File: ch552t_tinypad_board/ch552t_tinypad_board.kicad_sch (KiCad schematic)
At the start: 19 parts, among them J1 Conn_02x10_Odd_Even, J2 Conn_01x02_Pin, J3 USB_C_Receptacle_USB2.0, SW1 SW_Push, SW2 SW_Push, SW3 SW_Push, SW4 SW_Push, SW5 SW_Push, SW6 SW_Push, U1 CH552T

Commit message: feat: auto wiring and board outline
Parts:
- removed J2: Conn_01x02_Pin, Connector_PinHeader_2.54mm:PinHeader_1x02_P2.54mm_Vertical, symbol Connector:Conn_01x02_Pin
- added SW7: SW_Push, Library:SW_SPST_TVAF06_A020B_R, symbol Switch:SW_Push
- C1, C2: footprint Capacitor_SMD:C_0603_1608Metric_Pad1.08x0.95mm_HandSolder -> Library:C_SMD_0603_1608_Disc_DualUse
- D1: footprint LED_SMD:LED_0603_1608Metric_Pad1.05x0.95mm_HandSolder -> LED_THT:LED_D3.0mm
- R1, R2: footprint Resistor_SMD:R_0603_1608Metric_Pad0.98x0.95mm_HandSolder -> Library:R_SMD_0603_1608_THT_DIN0207_DualUse
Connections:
- net P1.4: no longer SW4.1
- net P3.0: now also SW4.1
- net at R2.2: now also SW7.2
- net P3.6 renamed D+
- net D+: now also SW7.1
- net P3.7 renamed D-

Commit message: feat: connect keys to MCU
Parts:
- removed H1, H2, H3, H4: MountingHole, MountingHole:MountingHole_3.2mm_M3, symbol Mechanical:MountingHole
- added H1, H2, H3, H4: MountingHole_Pad, MountingHole:MountingHole_3.2mm_M3_Pad_Via, symbol Mechanical:MountingHole_Pad
- renumbered J3 to J2
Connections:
- net GND: now also H1.1, H2.1, H3.1, H4.1
- net P1.0: no longer SW2.1
- net P1.1: now also SW6.1; no longer SW1.1
- net P1.5: no longer SW5.1
- net P1.6: no longer SW6.1
- net P1.7: no longer SW3.1
- net P3.1: now also SW5.1
- net P3.2: no longer D1.2 (A)
- net P3.3: now also SW1.1
- net P3.4: now also SW2.1
- net P3.5: now also SW3.1
- no-connect marks 4 -> 6

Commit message: fix: pulldown CC pins on USB-C
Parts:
- added R3, R4: R, Library:R_SMD_0603_1608_THT_DIN0207_DualUse, symbol Device:R
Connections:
- net GND: now also R3.2, R4.2
- net at J2.A5 (CC1): now also R4.1
- net at J2.B5 (CC2): now also R3.1
- no-connect marks 6 -> 4
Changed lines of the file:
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@@
   (junction (at 66.04 50.8) (diameter 0) (color 0 0 0 0)
   )
-  (no_connect (at 199.39 26.67))
   (no_connect (at 170.18 100.33))
   (no_connect (at 199.39 49.53))
-  (no_connect (at 199.39 29.21))
   (no_connect (at 199.39 52.07))
   (no_connect (at 176.53 90.17))
+  (wire (pts (xy 234.95 29.21) (xy 234.95 26.67))
+    (stroke (width 0) (type default))
+  )
   (wire (pts (xy 184.15 90.17) (xy 194.31 90.17))
     (stroke (width 0) (type default))
@@
     (stroke (width 0) (type default))
   )
+  (wire (pts (xy 226.06 36.83) (xy 226.06 39.37))
+    (stroke (width 0) (type default))
+  )
   (wire (pts (xy 210.82 82.55) (xy 144.78 82.55))
     (stroke (width 0) (type default))
@@
     (stroke (width 0) (type default))
   )
+  (wire (pts (xy 234.95 36.83) (xy 234.95 39.37))
+    (stroke (width 0) (type default))
+  )
+  (wire (pts (xy 234.95 26.67) (xy 199.39 26.67))
+    (stroke (width 0) (type default))
+  )
   (wire (pts (xy 184.15 59.69) (xy 184.15 62.23))
     (stroke (width 0) (type default))
@@
   )
   (wire (pts (xy 144.78 69.85) (xy 173.99 69.85))
+    (stroke (width 0) (type default))
+  )
+  (wire (pts (xy 199.39 29.21) (xy 226.06 29.21))
     (stroke (width 0) (type default))
   )
@@
     )
   )
+  (symbol (lib_id "power:GND") (at 226.06 39.37 0) (unit 1)
+    (in_bom yes) (on_board yes) (dnp no) (fields_autoplaced)
+    (property "Reference" "#PWR016" (at 226.06 45.72 0)
+      (effects (font (size 1.27 1.27)) hide)
+    )
+    (property "Value" "GND" (at 226.06 44.45 0)
+      (effects (font (size 1.27 1.27)))
+    )
+    (property "Footprint" "" (at 226.06 39.37 0)
+      (effects (font (size 1.27 1.27)) hide)
+    )
+    (property "Datasheet" "" (at 226.06 39.37 0)
+      (effects (font (size 1.27 1.27)) hide)
+    )
+    (pin "1")
+    (instances
+      (project "ch552t_tinypad_board"
+        (path "/12a9bd1e-67e4-4b41-b498-ff4d6b2646d2"
+          (reference "#PWR016") (unit 1)
+        )
+      )
+    )
+  )
   (symbol (lib_id "power:VCC") (at 173.99 69.85 0) (unit 1)
     (in_bom yes) (on_board yes) (dnp no) (fields_autoplaced)
@@
         (path "/56328475-aff9-4d2d-8d78-1ad1f91ab129"
           (reference "#PWR05") (unit 1)
+        )
+      )
+    )
+  )
+  (symbol (lib_id "Device:R") (at 234.95 33.02 0) (unit 1)
+    (in_bom yes) (on_board yes) (dnp no) (fields_autoplaced)
+    (property "Reference" "R4" (at 237.49 31.75 0)
+      (effects (font (size 1.27 1.27)) (justify left))
+    )
+    (property "Value" "R" (at 237.49 34.29 0)
+      (effects (font (size 1.27 1.27)) (justify left))
+    )
+    (property "Footprint" "Library:R_SMD_0603_1608_THT_DIN0207_DualUse" (at 233.172 33.02 90)
+      (effects (font (size 1.27 1.27)) hide)
+    )
+    (property "Datasheet" "~" (at 234.95 33.02 0)
+      (effects (font (size 1.27 1.27)) hide)
+    )
+    (pin "1")
+    (pin "2")
+    (instances
+      (project "ch552t_tinypad_board"
+        (path "/12a9bd1e-67e4-4b41-b498-ff4d6b2646d2"
+          (reference "R4") (unit 1)
         )
       )
@@
     )
   )
+  (symbol (lib_id "Device:R") (at 226.06 33.02 0) (unit 1)
+    (in_bom yes) (on_board yes) (dnp no) (fields_autoplaced)
+    (property "Reference" "R3" (at 228.6 31.75 0)
+      (effects (font (size 1.27 1.27)) (justify left))
+    )
+    (property "Value" "R" (at 228.6 34.29 0)
+      (effects (font (size 1.27 1.27)) (justify left))
+    )
+    (property "Footprint" "Library:R_SMD_0603_1608_THT_DIN0207_DualUse" (at 224.282 33.02 90)
+      (effects (font (size 1.27 1.27)) hide)
+    )
+    (property "Datasheet" "~" (at 226.06 33.02 0)
+      (effects (font (size 1.27 1.27)) hide)
+    )
+    (pin "1")
+    (pin "2")
+    (instances
+      (project "ch552t_tinypad_board"
+        (path "/12a9bd1e-67e4-4b41-b498-ff4d6b2646d2"
+          (reference "R3") (unit 1)
+        )
+      )
+    )
+  )
   (symbol (lib_id "Switch:SW_Push") (at 43.18 24.13 0) (unit 1)
     (in_bom yes) (on_board yes) (dnp no) (fields_autoplaced)
@@
         )
       )
+    )
+  )
+  (symbol (lib_id "power:GND") (at 234.95 39.37 0) (unit 1)
+    (in_bom yes) (on_board yes) (dnp no) (fields_autoplaced)
+    (property "Reference" "#PWR017" (at 234.95 45.72 0)
+      (effects (font (size 1.27 1.27)) hide)
+    )
+    (property "Value" "GND" (at 234.95 44.45 0)
+      (effects (font (size 1.27 1.27)))
+    )
+    (property "Footprint" "" (at 234.95 39.37 0)
+      (effects (font (size 1.27 1.27)) hide)
+    )
+    (property "Datasheet" "" (at 234.95 39.37 0)
+      (effects (font (size 1.27 1.27)) hide)
+    )
+    (pin "1")
+    (instances
+      (project "ch552t_tinypad_board"
+        (path "/12a9bd1e-67e4-4b41-b498-ff4d6b2646d2"
+          (reference "#PWR017") (unit 1)
+        )
+      )

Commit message: feat: silkscreen artwork(?)
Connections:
- net P1.0: now also D1.2 (A)
- no-connect marks 4 -> 3
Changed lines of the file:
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@@
   (no_connect (at 199.39 49.53))
   (no_connect (at 199.39 52.07))
-  (no_connect (at 176.53 90.17))
   (wire (pts (xy 234.95 29.21) (xy 234.95 26.67))
     (stroke (width 0) (type default))
@@
     (effects (font (size 1.27 1.27)) (justify right bottom))
   )
+  (label "P1.0" (at 176.53 90.17 180) (fields_autoplaced)
+    (effects (font (size 1.27 1.27)) (justify right bottom))
+  )
   (label "P1.5" (at 62.23 111.76 180) (fields_autoplaced)
     (effects (font (size 1.27 1.27)) (justify right bottom))
@@
     (effects (font (size 1.27 1.27)) (justify right bottom))
   )
-  (label "P3.2" (at 170.18 100.33 180) (fields_autoplaced)
-    (effects (font (size 1.27 1.27)) (justify right bottom))
-  )
   (label "P1.3" (at 144.78 77.47 0) (fields_autoplaced)
     (effects (font (size 1.27 1.27)) (justify left bottom))
@@
     )
   )
-  (symbol (lib_id "ch552:CH552T") (at 118.11 78.74 0) (unit 1)
-    (in_bom yes) (on_board yes) (dnp no) (fields_autoplaced)
-    (property "Reference" "U1" (at 117.475 59.69 0)
-      (effects (font (size 1.27 1.27)))
-    )
-    (property "Value" "CH552T" (at 117.475 62.23 0)
-      (effects (font (size 1.27 1.27)))
-    )
-    (property "Footprint" "Package_SO:TSSOP-20_4.4x6.5mm_P0.65mm" (at 118.11 96.52 0)
-      (effects (font (size 1.27 1.27)) hide)
-    )
-    (property "Datasheet" "https://akizukidenshi.com/download/ds/wch/CH552.pdf" (at 116.84 93.98 0)
-      (effects (font (size 1.27 1.27)) hide)
-    )
-    (pin "1")
-    (pin "10")
-    (pin "11")
-    (pin "12")
-    (pin "13")
-    (pin "14")
-    (pin "15")
-    (pin "16")
-    (pin "17")
-    (pin "18")
-    (pin "19")
-    (pin "2")
-    (pin "20")
-    (pin "3")
-    (pin "4")
-    (pin "5")
-    (pin "6")
-    (pin "7")
-    (pin "8")
-    (pin "9")
-    (instances
-      (project "ch552t_tinypad_board"
-        (path "/12a9bd1e-67e4-4b41-b498-ff4d6b2646d2"
-          (reference "U1") (unit 1)
-        )
-      )
-    )
-  )
   (symbol (lib_id "Switch:SW_Push") (at 44.45 45.72 0) (unit 1)
     (in_bom yes) (on_board yes) (dnp no) (fields_autoplaced)
@@
         (path "/12a9bd1e-67e4-4b41-b498-ff4d6b2646d2"
           (reference "#PWR04") (unit 1)
+        )
+      )
+    )
+  )
+  (symbol (lib_id "Graphic:Logo_Open_Hardware_Small") (at 43.18 179.07 0) (unit 1)
+    (in_bom no) (on_board no) (dnp no) (fields_autoplaced)
+    (property "Reference" "#SYM1" (at 43.18 172.085 0)
+      (effects (font (size 1.27 1.27)) hide)
+    )
+    (property "Value" "Logo_Open_Hardware_Small" (at 43.18 184.785 0)
+      (effects (font (size 1.27 1.27)) hide)
+    )
+    (property "Footprint" "" (at 43.18 179.07 0)
+      (effects (font (size 1.27 1.27)) hide)
+    )
+    (property "Datasheet" "~" (at 43.18 179.07 0)
+      (effects (font (size 1.27 1.27)) hide)
+    )
+    (property "Sim.Enable" "0" (at 43.18 179.07 0)
+      (effects (font (size 1.27 1.27)) hide)
+    )
+    (instances
+      (project "ch552t_tinypad_board"
+        (path "/12a9bd1e-67e4-4b41-b498-ff4d6b2646d2"
+          (reference "#SYM1") (unit 1)
         )
       )
@@
         )
       )
+    )
+  )
+  (symbol (lib_id "ch552:CH552T") (at 118.11 78.74 0) (unit 1)
+    (in_bom yes) (on_board yes) (dnp no) (fields_autoplaced)
+    (property "Reference" "U1" (at 117.475 59.69 0)
+      (effects (font (size 1.27 1.27)))
+    )
+    (property "Value" "CH552T" (at 117.475 62.23 0)
+      (effects (font (size 1.27 1.27)))
+    )
+    (property "Footprint" "Package_SO:TSSOP-20_4.4x6.5mm_P0.65mm" (at 118.11 96.52 0)
+      (effects (font (size 1.27 1.27)) hide)
+    )
+    (property "Datasheet" "https://akizukidenshi.com/download/ds/wch/CH552.pdf" (at 116.84 93.98 0)
+      (effects (font (size 1.27 1.27)) hide)
+    )
+    (pin "1")
+    (pin "10")
+    (pin "11")
+    (pin "12")
+    (pin "13")
+    (pin "14")
+    (pin "15")
+    (pin "16")
+    (pin "17")
+    (pin "18")
+    (pin "19")
+    (pin "2")
+    (pin "20")
+    (pin "3")
+    (pin "4")
+    (pin "5")
+    (pin "6")
+    (pin "7")
+    (pin "8")
+    (pin "9")
+    (instances
+      (project "ch552t_tinypad_board"
+        (path "/12a9bd1e-67e4-4b41-b498-ff4d6b2646d2"
+          (reference "U1") (unit 1)
+        )
+      )

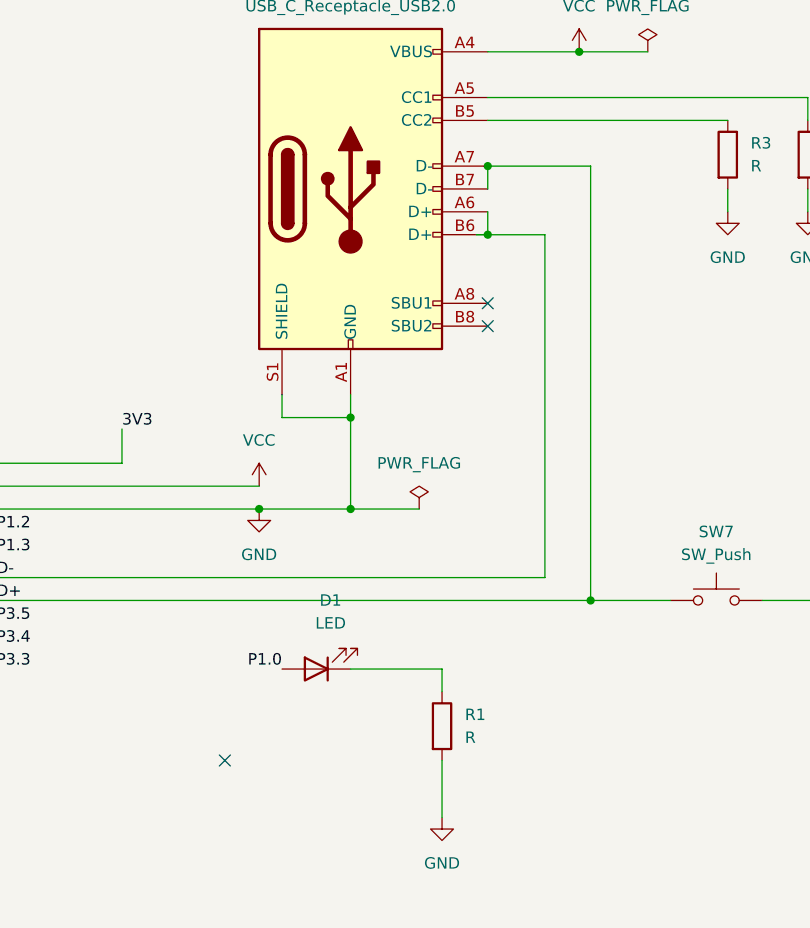
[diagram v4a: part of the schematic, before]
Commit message: hotfix: replace swapped USB differential pair
pcb is not fixed
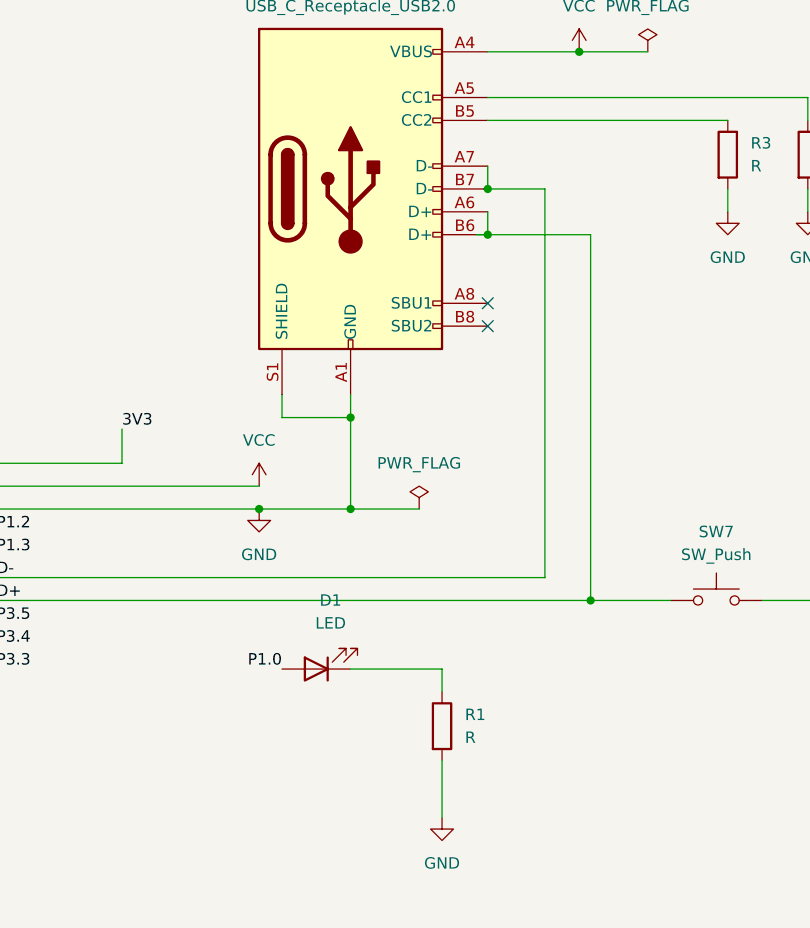
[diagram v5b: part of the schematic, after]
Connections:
- net D+: now also J2.A6 (D+), J2.B6 (D+); no longer J2.A7 (D-), J2.B7 (D-)
- net D-: now also J2.A7 (D-), J2.B7 (D-); no longer J2.A6 (D+), J2.B6 (D+)
- no-connect marks 3 -> 2
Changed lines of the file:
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@@
   (junction (at 184.15 62.23) (diameter 0) (color 0 0 0 0)
+  )
+  (junction (at 199.39 36.83) (diameter 0) (color 0 0 0 0)
   )
   (junction (at 64.77 29.21) (diameter 0) (color 0 0 0 0)
@@
   )
   (junction (at 209.55 21.59) (diameter 0) (color 0 0 0 0)
-  )
-  (junction (at 199.39 34.29) (diameter 0) (color 0 0 0 0)
   )
   (junction (at 210.82 82.55) (diameter 0) (color 0 0 0 0)
@@
   (junction (at 66.04 50.8) (diameter 0) (color 0 0 0 0)
   )
-  (no_connect (at 170.18 100.33))
   (no_connect (at 199.39 49.53))
   (no_connect (at 199.39 52.07))
@@
     (stroke (width 0) (type default))
   )
+  (wire (pts (xy 199.39 41.91) (xy 210.82 41.91))
+    (stroke (width 0) (type default))
+  )
   (wire (pts (xy 210.82 82.55) (xy 144.78 82.55))
     (stroke (width 0) (type default))
@@
     (stroke (width 0) (type default))
   )
-  (wire (pts (xy 199.39 34.29) (xy 210.82 34.29))
+  (wire (pts (xy 199.39 36.83) (xy 205.74 36.83))
     (stroke (width 0) (type default))
   )
@@
     (stroke (width 0) (type default))
   )
-  (wire (pts (xy 205.74 80.01) (xy 205.74 41.91))
+  (wire (pts (xy 205.74 36.83) (xy 205.74 80.01))
     (stroke (width 0) (type default))
   )
@@
     (stroke (width 0) (type default))
   )
-  (wire (pts (xy 210.82 34.29) (xy 210.82 82.55))
+  (wire (pts (xy 210.82 41.91) (xy 210.82 82.55))
     (stroke (width 0) (type default))
   )
@@
     (stroke (width 0) (type default))
   )
-  (wire (pts (xy 199.39 41.91) (xy 205.74 41.91))
-    (stroke (width 0) (type default))
-  )

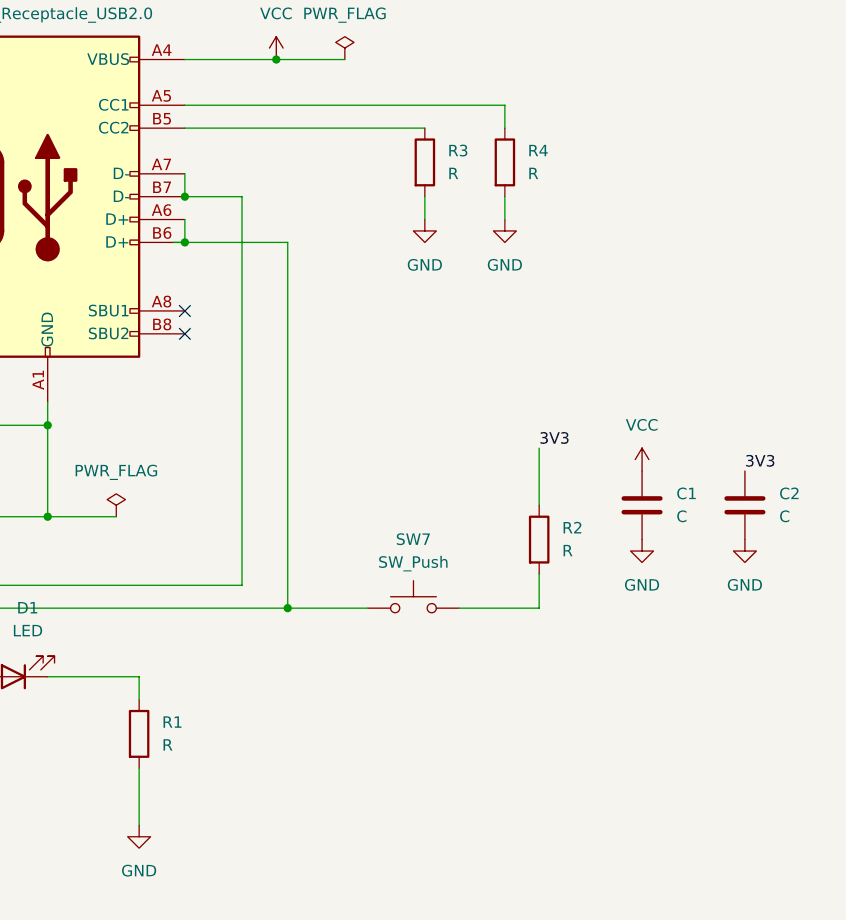
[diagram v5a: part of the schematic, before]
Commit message: fix: rewire USB diff pair
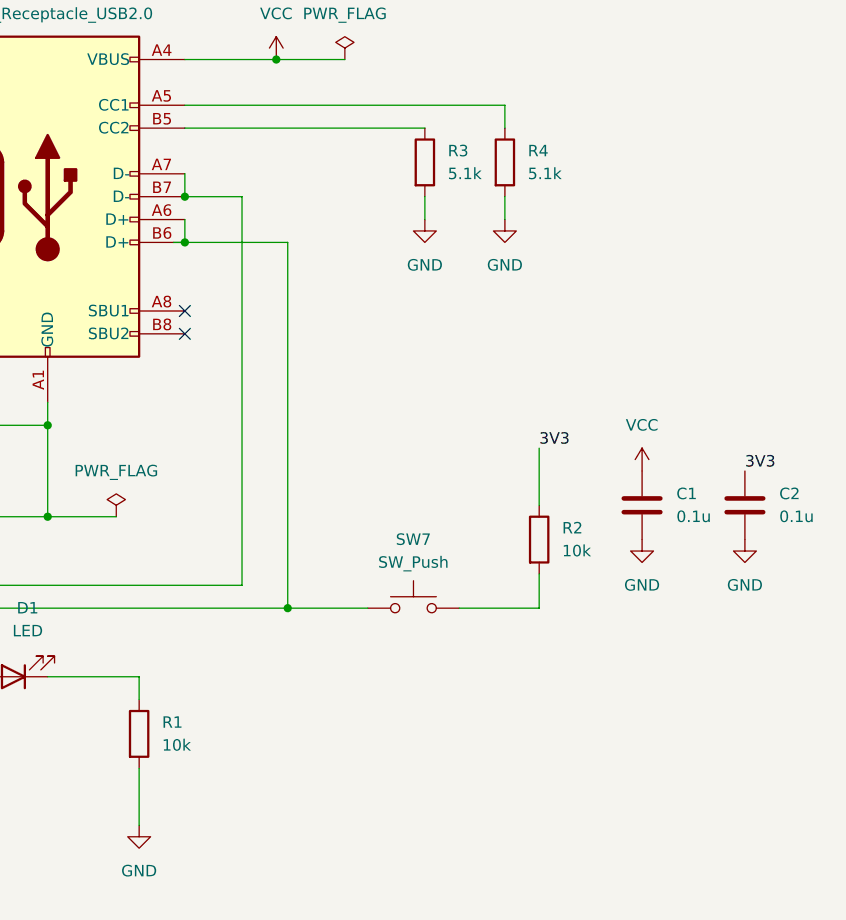
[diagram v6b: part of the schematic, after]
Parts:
- C1, C2: value C -> 0.1u
- R1, R2: value R -> 10k
- R3, R4: value R -> 5.1k
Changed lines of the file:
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@@
       (effects (font (size 1.27 1.27)) (justify left))
     )
-    (property "Value" "R" (at 196.85 97.79 0)
+    (property "Value" "10k" (at 196.85 97.79 0)
       (effects (font (size 1.27 1.27)) (justify left))
     )
@@
       (effects (font (size 1.27 1.27)) (justify left))
     )
-    (property "Value" "C" (at 265.43 72.39 0)
+    (property "Value" "0.1u" (at 265.43 72.39 0)
       (effects (font (size 1.27 1.27)) (justify left))
     )
@@
       (effects (font (size 1.27 1.27)) (justify left))
     )
-    (property "Value" "R" (at 237.49 34.29 0)
+    (property "Value" "5.1k" (at 237.49 34.29 0)
       (effects (font (size 1.27 1.27)) (justify left))
     )
@@
       (effects (font (size 1.27 1.27)) (justify left))
     )
-    (property "Value" "R" (at 241.3 76.2 0)
+    (property "Value" "10k" (at 241.3 76.2 0)
       (effects (font (size 1.27 1.27)) (justify left))
     )
@@
       (effects (font (size 1.27 1.27)) (justify left))
     )
-    (property "Value" "R" (at 228.6 34.29 0)
+    (property "Value" "5.1k" (at 228.6 34.29 0)
       (effects (font (size 1.27 1.27)) (justify left))
     )
@@
       (effects (font (size 1.27 1.27)) (justify left))
     )
-    (property "Value" "C" (at 254 72.39 0)
-      (effects (font (size 1.27 1.27)) (justify left))
-    )
+    (property "Value" "0.1u" (at 254 72.39 0)
+      (effects (font (size 1.27 1.27)) (justify left))
+    )
